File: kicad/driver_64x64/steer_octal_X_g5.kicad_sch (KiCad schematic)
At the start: 66 parts

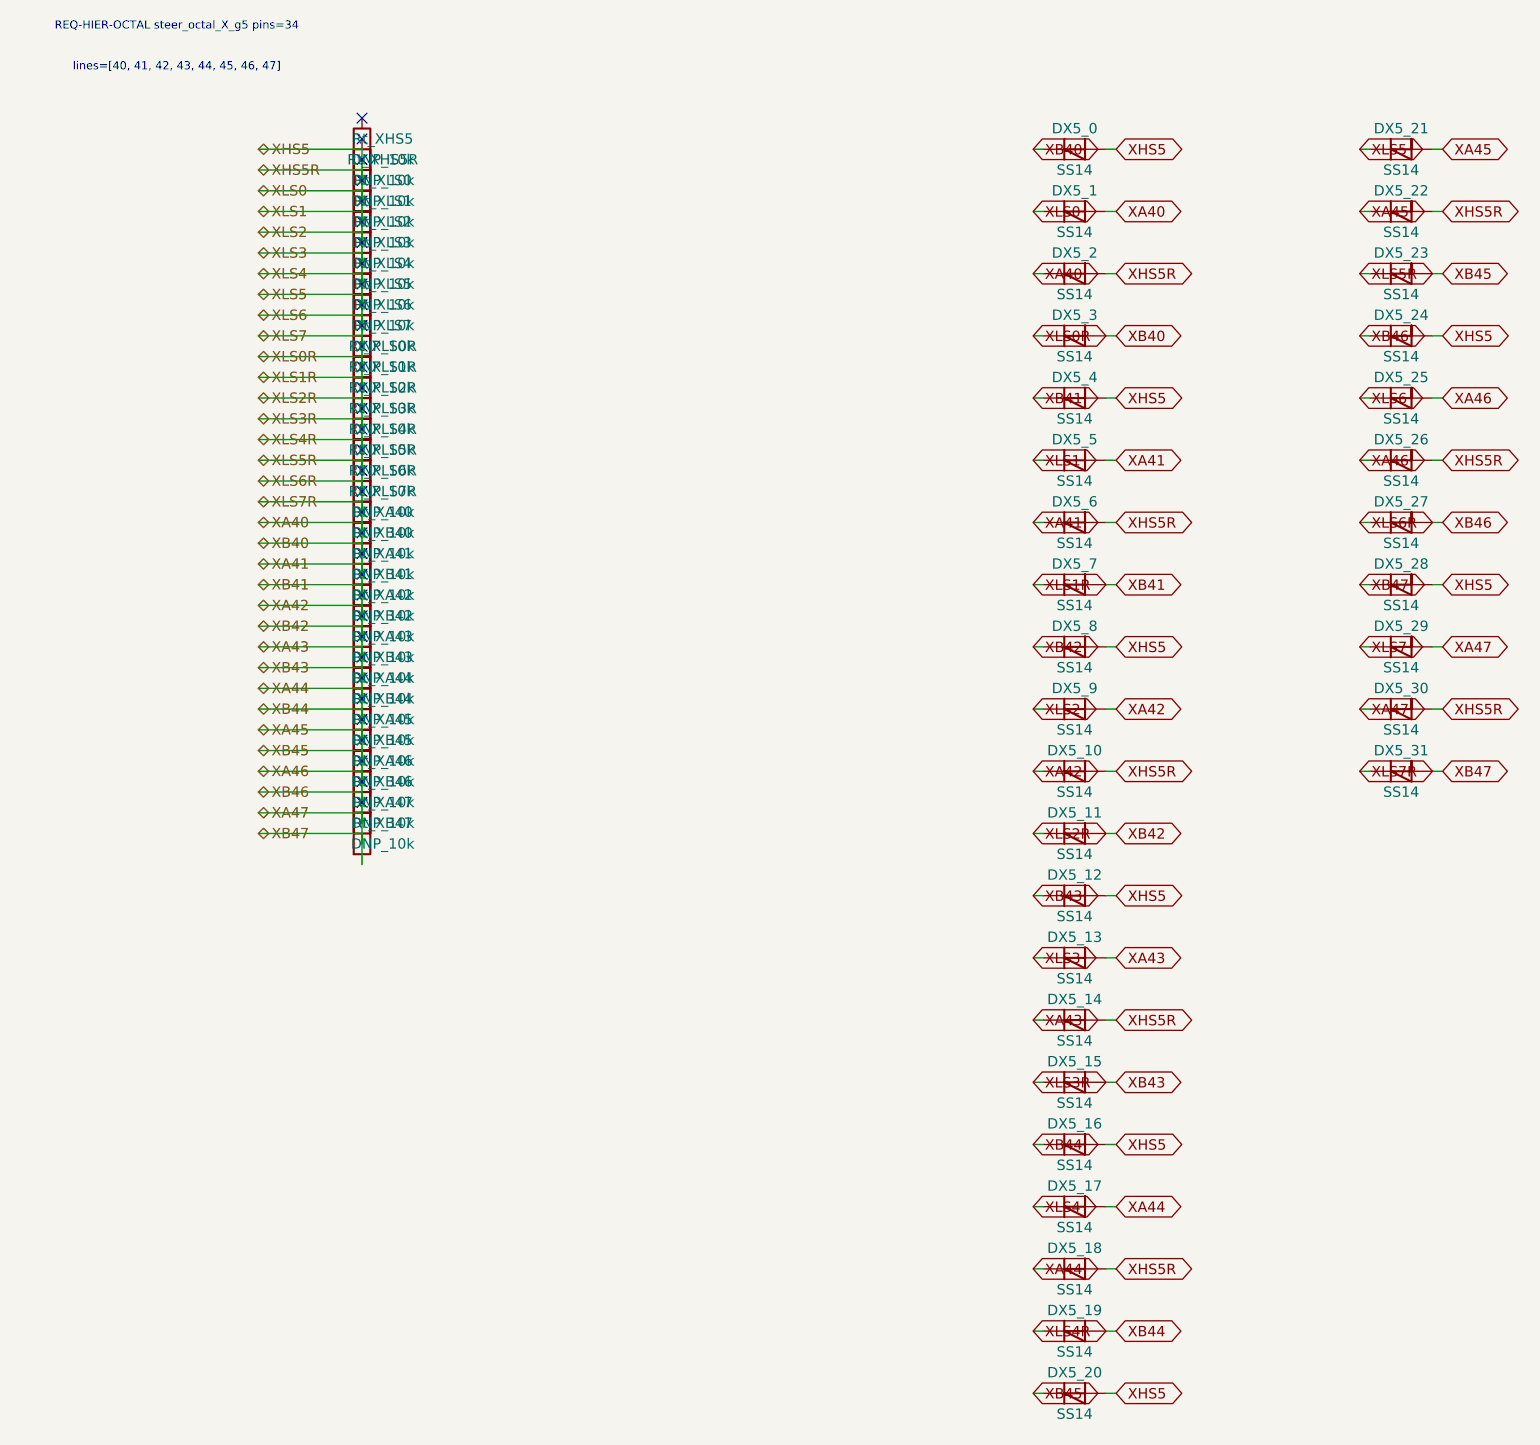
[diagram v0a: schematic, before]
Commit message: logical seperation into host and multiple decode/drive/steering boards
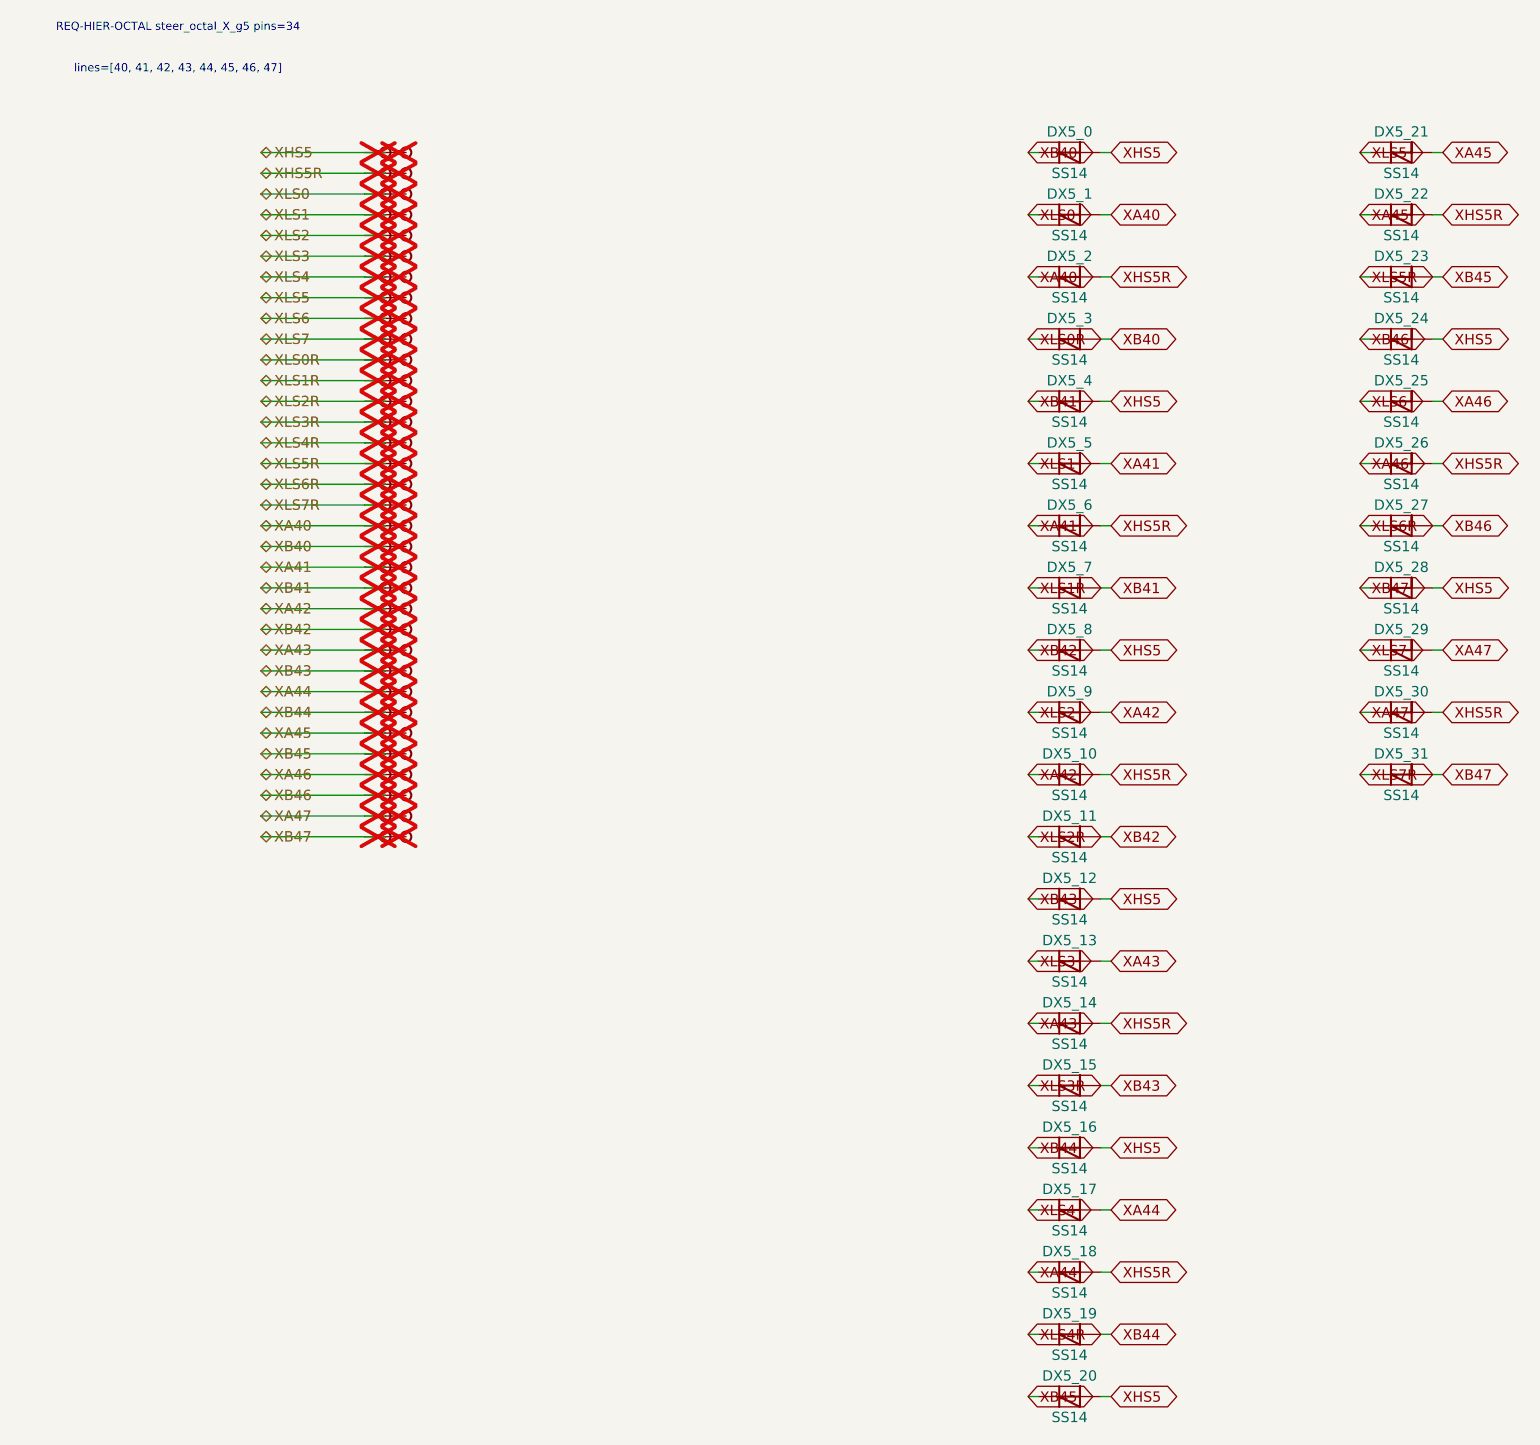
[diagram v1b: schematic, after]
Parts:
- removed Rt_XA40, Rt_XA41, Rt_XA42, Rt_XA43, Rt_XA44, Rt_XA45, Rt_XA46, Rt_XA47, Rt_XB40, Rt_XB41, Rt_XB42, Rt_XB43, Rt_XB44, Rt_XB45, Rt_XB46, Rt_XB47, Rt_XHS5, Rt_XHS5R, Rt_XLS0, Rt_XLS0R, Rt_XLS1, Rt_XLS1R, Rt_XLS2, Rt_XLS2R, Rt_XLS3, Rt_XLS3R, Rt_XLS4, Rt_XLS4R, Rt_XLS5, Rt_XLS5R, Rt_XLS6, Rt_XLS6R, Rt_XLS7, Rt_XLS7R: DNP_10k, symbol Device:R
- added TP_XA40, TP_XA40b, TP_XA41, TP_XA41b, TP_XA42, TP_XA42b, TP_XA43, TP_XA43b, TP_XA44, TP_XA44b, TP_XA45, TP_XA45b, TP_XA46, TP_XA46b, TP_XA47, TP_XA47b, TP_XB40, TP_XB40b, TP_XB41, TP_XB41b, TP_XB42, TP_XB42b, TP_XB43, TP_XB43b, TP_XB44, TP_XB44b, TP_XB45, TP_XB45b, TP_XB46, TP_XB46b, TP_XB47, TP_XB47b, TP_XHS5, TP_XHS5R, TP_XHS5Rb, TP_XHS5b, TP_XLS0, TP_XLS0R, TP_XLS0Rb, TP_XLS0b, TP_XLS1, TP_XLS1R, TP_XLS1Rb, TP_XLS1b, TP_XLS2, TP_XLS2R, TP_XLS2Rb, TP_XLS2b, TP_XLS3, TP_XLS3R, TP_XLS3Rb, TP_XLS3b, TP_XLS4, TP_XLS4R, TP_XLS4Rb, TP_XLS4b, TP_XLS5, TP_XLS5R, TP_XLS5Rb, TP_XLS5b, TP_XLS6, TP_XLS6R, TP_XLS6Rb, TP_XLS6b, TP_XLS7, TP_XLS7R, TP_XLS7Rb, TP_XLS7b: Stub, symbol CMR:Stub
- DX5_0, DX5_1, DX5_10, DX5_11, DX5_12, DX5_13, DX5_14, DX5_15, DX5_16, DX5_17, DX5_18, DX5_19, DX5_2, DX5_20, DX5_21, DX5_22, DX5_23, DX5_24, DX5_25, DX5_26, DX5_27, DX5_28, DX5_29, DX5_3, DX5_30, DX5_31, DX5_4, DX5_5, DX5_6, DX5_7, DX5_8, DX5_9: symbol Device:D_Schottky -> CMR:D_Schottky
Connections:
- net XA40: now also TP_XA40.1, TP_XA40b.1; no longer DX5_0.1 (K), DX5_0.2 (A), DX5_1.1 (K), DX5_10.1 (K), DX5_10.2 (A), DX5_11.1 (K), DX5_11.2 (A), DX5_12.1 (K), DX5_12.2 (A), DX5_13.1 (K), DX5_13.2 (A), DX5_14.1 (K), DX5_14.2 (A), DX5_15.1 (K), DX5_15.2 (A), DX5_16.1 (K), DX5_16.2 (A), DX5_17.1 (K), DX5_17.2 (A), DX5_18.1 (K), DX5_18.2 (A), DX5_19.1 (K), DX5_19.2 (A), DX5_2.2 (A), DX5_20.1 (K), DX5_20.2 (A), DX5_21.1 (K), DX5_21.2 (A), DX5_22.1 (K), DX5_22.2 (A), DX5_23.1 (K), DX5_23.2 (A), DX5_24.1 (K), DX5_24.2 (A), DX5_25.1 (K), DX5_25.2 (A), DX5_26.1 (K), DX5_26.2 (A), DX5_27.1 (K), DX5_27.2 (A), DX5_28.1 (K), DX5_28.2 (A), DX5_29.1 (K), DX5_29.2 (A), DX5_3.1 (K), DX5_3.2 (A), DX5_30.1 (K), DX5_30.2 (A), DX5_31.1 (K), DX5_31.2 (A), DX5_4.1 (K), DX5_4.2 (A), DX5_5.1 (K), DX5_5.2 (A), DX5_6.1 (K), DX5_6.2 (A), DX5_7.1 (K), DX5_7.2 (A), DX5_8.1 (K), DX5_8.2 (A), DX5_9.1 (K), DX5_9.2 (A)
- new net XA41: DX5_5.2 (A), DX5_6.1 (K), TP_XA41.1, TP_XA41b.1
- new net XA42: DX5_10.1 (K), DX5_9.2 (A), TP_XA42.1, TP_XA42b.1
- new net XA43: DX5_13.2 (A), DX5_14.1 (K), TP_XA43.1, TP_XA43b.1
- new net XA44: DX5_17.2 (A), DX5_18.1 (K), TP_XA44.1, TP_XA44b.1
- new net XA45: DX5_21.2 (A), DX5_22.1 (K), TP_XA45.1, TP_XA45b.1
- new net XA46: DX5_25.2 (A), DX5_26.1 (K), TP_XA46.1, TP_XA46b.1
- new net XA47: DX5_29.2 (A), DX5_30.1 (K), TP_XA47.1, TP_XA47b.1
- new net XB40: DX5_0.1 (K), DX5_3.2 (A), TP_XB40.1, TP_XB40b.1
- new net XB41: DX5_4.1 (K), DX5_7.2 (A), TP_XB41.1, TP_XB41b.1
- new net XB42: DX5_11.2 (A), DX5_8.1 (K), TP_XB42.1, TP_XB42b.1
- new net XB43: DX5_12.1 (K), DX5_15.2 (A), TP_XB43.1, TP_XB43b.1
- new net XB44: DX5_16.1 (K), DX5_19.2 (A), TP_XB44.1, TP_XB44b.1
- new net XB45: DX5_20.1 (K), DX5_23.2 (A), TP_XB45.1, TP_XB45b.1
- new net XB46: DX5_24.1 (K), DX5_27.2 (A), TP_XB46.1, TP_XB46b.1
- new net XB47: DX5_28.1 (K), DX5_31.2 (A), TP_XB47.1, TP_XB47b.1
- new net XHS5: DX5_0.2 (A), DX5_12.2 (A), DX5_16.2 (A), DX5_20.2 (A), DX5_24.2 (A), DX5_28.2 (A), DX5_4.2 (A), DX5_8.2 (A), TP_XHS5.1, TP_XHS5b.1
- new net XHS5R: DX5_10.2 (A), DX5_14.2 (A), DX5_18.2 (A), DX5_2.2 (A), DX5_22.2 (A), DX5_26.2 (A), DX5_30.2 (A), DX5_6.2 (A), TP_XHS5R.1, TP_XHS5Rb.1
- new net XLS0: DX5_1.1 (K), TP_XLS0.1, TP_XLS0b.1
- new net XLS0R: DX5_3.1 (K), TP_XLS0R.1, TP_XLS0Rb.1
- new net XLS1: DX5_5.1 (K), TP_XLS1.1, TP_XLS1b.1
- new net XLS1R: DX5_7.1 (K), TP_XLS1R.1, TP_XLS1Rb.1
- new net XLS2: DX5_9.1 (K), TP_XLS2.1, TP_XLS2b.1
- new net XLS2R: DX5_11.1 (K), TP_XLS2R.1, TP_XLS2Rb.1
- new net XLS3: DX5_13.1 (K), TP_XLS3.1, TP_XLS3b.1
- new net XLS3R: DX5_15.1 (K), TP_XLS3R.1, TP_XLS3Rb.1
- new net XLS4: DX5_17.1 (K), TP_XLS4.1, TP_XLS4b.1
- new net XLS4R: DX5_19.1 (K), TP_XLS4R.1, TP_XLS4Rb.1
- new net XLS5: DX5_21.1 (K), TP_XLS5.1, TP_XLS5b.1
- new net XLS5R: DX5_23.1 (K), TP_XLS5R.1, TP_XLS5Rb.1
- new net XLS6: DX5_25.1 (K), TP_XLS6.1, TP_XLS6b.1
- new net XLS6R: DX5_27.1 (K), TP_XLS6R.1, TP_XLS6Rb.1
- new net XLS7: DX5_29.1 (K), TP_XLS7.1, TP_XLS7b.1
- new net XLS7R: DX5_31.1 (K), TP_XLS7R.1, TP_XLS7Rb.1
- no-connect marks 34 -> 0
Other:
- moved on the sheet: DX5_0, DX5_1, DX5_10, DX5_11, DX5_12, DX5_13, DX5_14, DX5_15, DX5_16, DX5_17, DX5_18, DX5_19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
